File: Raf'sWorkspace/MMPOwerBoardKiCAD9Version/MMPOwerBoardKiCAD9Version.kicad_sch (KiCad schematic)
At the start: 102 parts, among them J1 TYPE-C-31-M-04, J2 Conn_02x16_Odd_Even, J3 Conn_01x02, Q1 SS8050, SW1 SS-12D11-G050, U1 HUSB237, U10 TPS22917DBVR, U11 AMS1117-5.0, U2 TP4056-42-ESOP8, U3 DRV8833PWPR, U4 TPS63802DLAR, U5 TPS22917DBVR, U6 TPS61236PRWLR, U7 INA219AIDR, U9 DRV8833PWPR

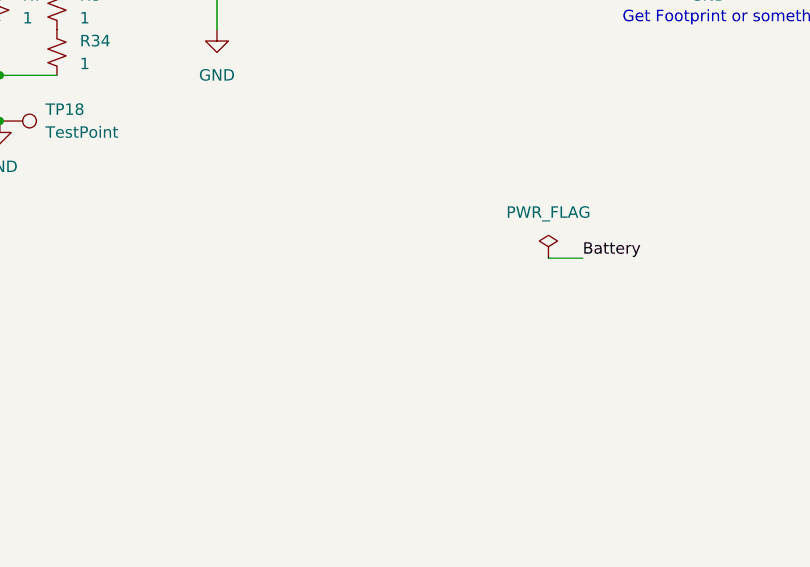
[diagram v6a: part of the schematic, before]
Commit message: Added Drill hole space x1 to hold up board
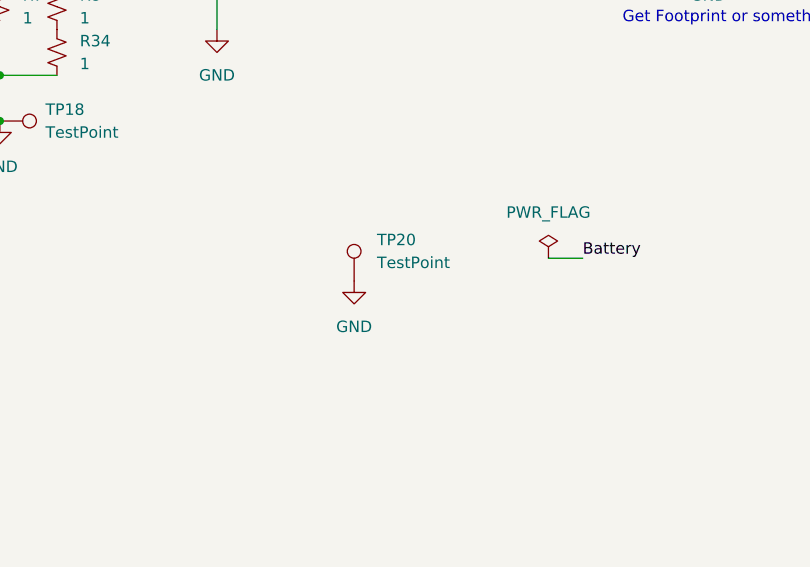
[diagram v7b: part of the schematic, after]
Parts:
- added TP20: TestPoint, TestPoint:TestPoint_Pad_4.0x4.0mm, symbol Connector:TestPoint
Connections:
- net GND: now also TP20.1
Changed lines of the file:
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@@
+	)
+	(symbol
+		(lib_id "power:GND")
+		(at 344.17 234.95 0)
+		(unit 1)
+		(exclude_from_sim no)
+		(in_bom yes)
+		(on_board yes)
+		(dnp no)
+		(fields_autoplaced yes)
+		(property "Reference" "#PWR032"
+			(at 344.17 241.3 0)
+			(effects
+				(font
+					(size 1.27 1.27)
+				)
+				(hide yes)
+			)
+		)
+		(property "Value" "GND"
+			(at 344.17 240.03 0)
+			(effects
+				(font
+					(size 1.27 1.27)
+				)
+			)
+		)
+		(property "Footprint" ""
+			(at 344.17 234.95 0)
+			(effects
+				(font
+					(size 1.27 1.27)
+				)
+				(hide yes)
+			)
+		)
+		(property "Datasheet" ""
+			(at 344.17 234.95 0)
+			(effects
+				(font
+					(size 1.27 1.27)
+				)
+				(hide yes)
+			)
+		)
+		(property "Description" "Power symbol creates a global label with name \"GND\" , ground"
+			(at 344.17 234.95 0)
+			(effects
+				(font
+					(size 1.27 1.27)
+				)
+				(hide yes)
+			)
+		)
+		(pin "1"
+		)
+		(instances
+			(project "MMPOwerBoardKiCAD9Version"
+				(path "/23b21de8-5207-4e61-b362-6de1163568fa"
+					(reference "#PWR032")
+					(unit 1)
+				)
+			)
+		)
 	)
 	(symbol
@@
 					(unit 1)
 				)
+			)
+		)
+	)
+	(symbol
+		(lib_id "Connector:TestPoint")
+		(at 344.17 234.95 0)
+		(unit 1)
+		(exclude_from_sim no)
+		(in_bom yes)
+		(on_board yes)
+		(dnp no)
+		(fields_autoplaced yes)
+		(property "Reference" "TP20"
+			(at 346.71 230.3779 0)
+			(effects
+				(font
+					(size 1.27 1.27)
+				)
+				(justify left)
+			)
+		)
+		(property "Value" "TestPoint"
+			(at 346.71 232.9179 0)
+			(effects
+				(font
+					(size 1.27 1.27)
+				)
+				(justify left)
+			)
+		)
+		(property "Footprint" "TestPoint:TestPoint_Pad_4.0x4.0mm"
+			(at 349.25 234.95 0)
+			(effects
+				(font
+					(size 1.27 1.27)
+				)
+				(hide yes)
+			)
+		)
+		(property "Datasheet" "~"
+			(at 349.25 234.95 0)
+			(effects
+				(font
+					(size 1.27 1.27)
+				)
+				(hide yes)
+			)
+		)
+		(property "Description" "test point"
+			(at 344.17 234.95 0)
+			(effects
+				(font
+					(size 1.27 1.27)
+				)
+				(hide yes)
+			)
+		)
+		(pin "1"
+		)
+		(instances
+			(project ""
+				(path "/23b21de8-5207-4e61-b362-6de1163568fa"
+					(reference "TP20")
+					(unit 1)
+				)
